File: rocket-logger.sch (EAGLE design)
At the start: 57 parts, among them IC1 CC430F513X, U1 MAX1555, X1 0896BM15A0001, X2 USB-MICROB, X3 SMA-142-0701-801/806

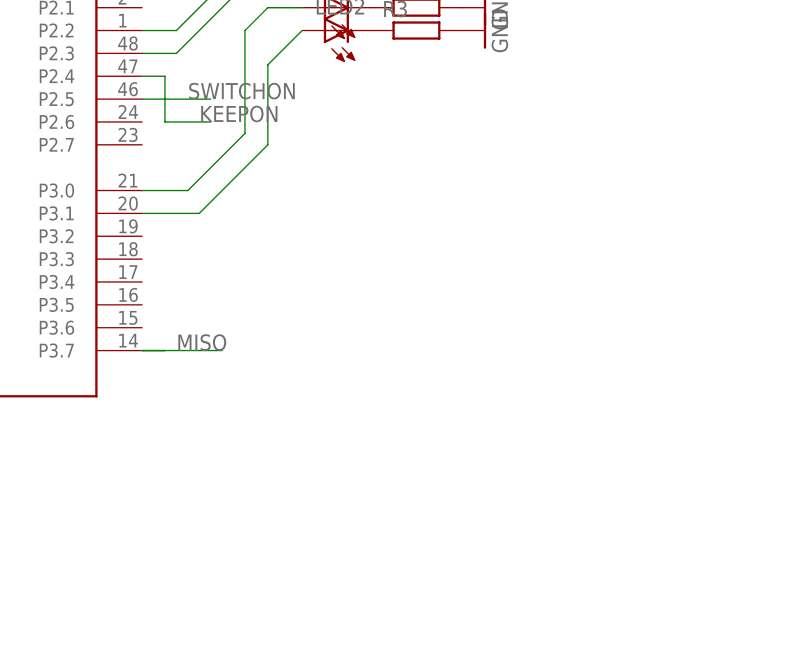
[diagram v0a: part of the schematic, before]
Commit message: now with added flash
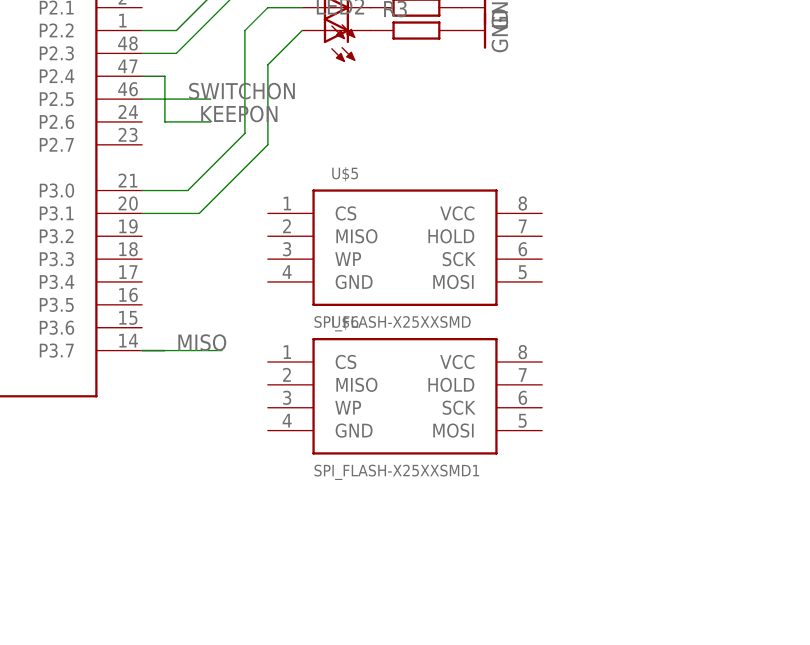
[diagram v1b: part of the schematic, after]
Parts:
- added U$5: SPI_FLASH-X25XXSMD, SparkFun:SPI_FLASH-X25XXSMD
- added U$6: SPI_FLASH-X25XXSMD1, SparkFun:SPI_FLASH-X25XXSMD1
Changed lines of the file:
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@@
 <part name="D4" library="diode" deviceset="DIODE-" device="SOD523"/>
 <part name="R5" library="rcl" deviceset="R-EU_" device="R0402"/>
+<part name="U$5" library="SparkFun" deviceset="SPI_FLASH-X25XX" device="SMD"/>
+<part name="U$6" library="SparkFun" deviceset="SPI_FLASH-X25XX" device="SMD1"/>
 </parts>
 <sheets>
@@
 <instance part="D4" gate="G$1" x="160.02" y="209.55" rot="R180"/>
 <instance part="R5" gate="G$1" x="168.91" y="191.77" rot="R180"/>
+<instance part="U$5" gate="G$1" x="95.25" y="124.46"/>
+<instance part="U$6" gate="G$1" x="95.25" y="107.95"/>
 </instances>
 <busses>

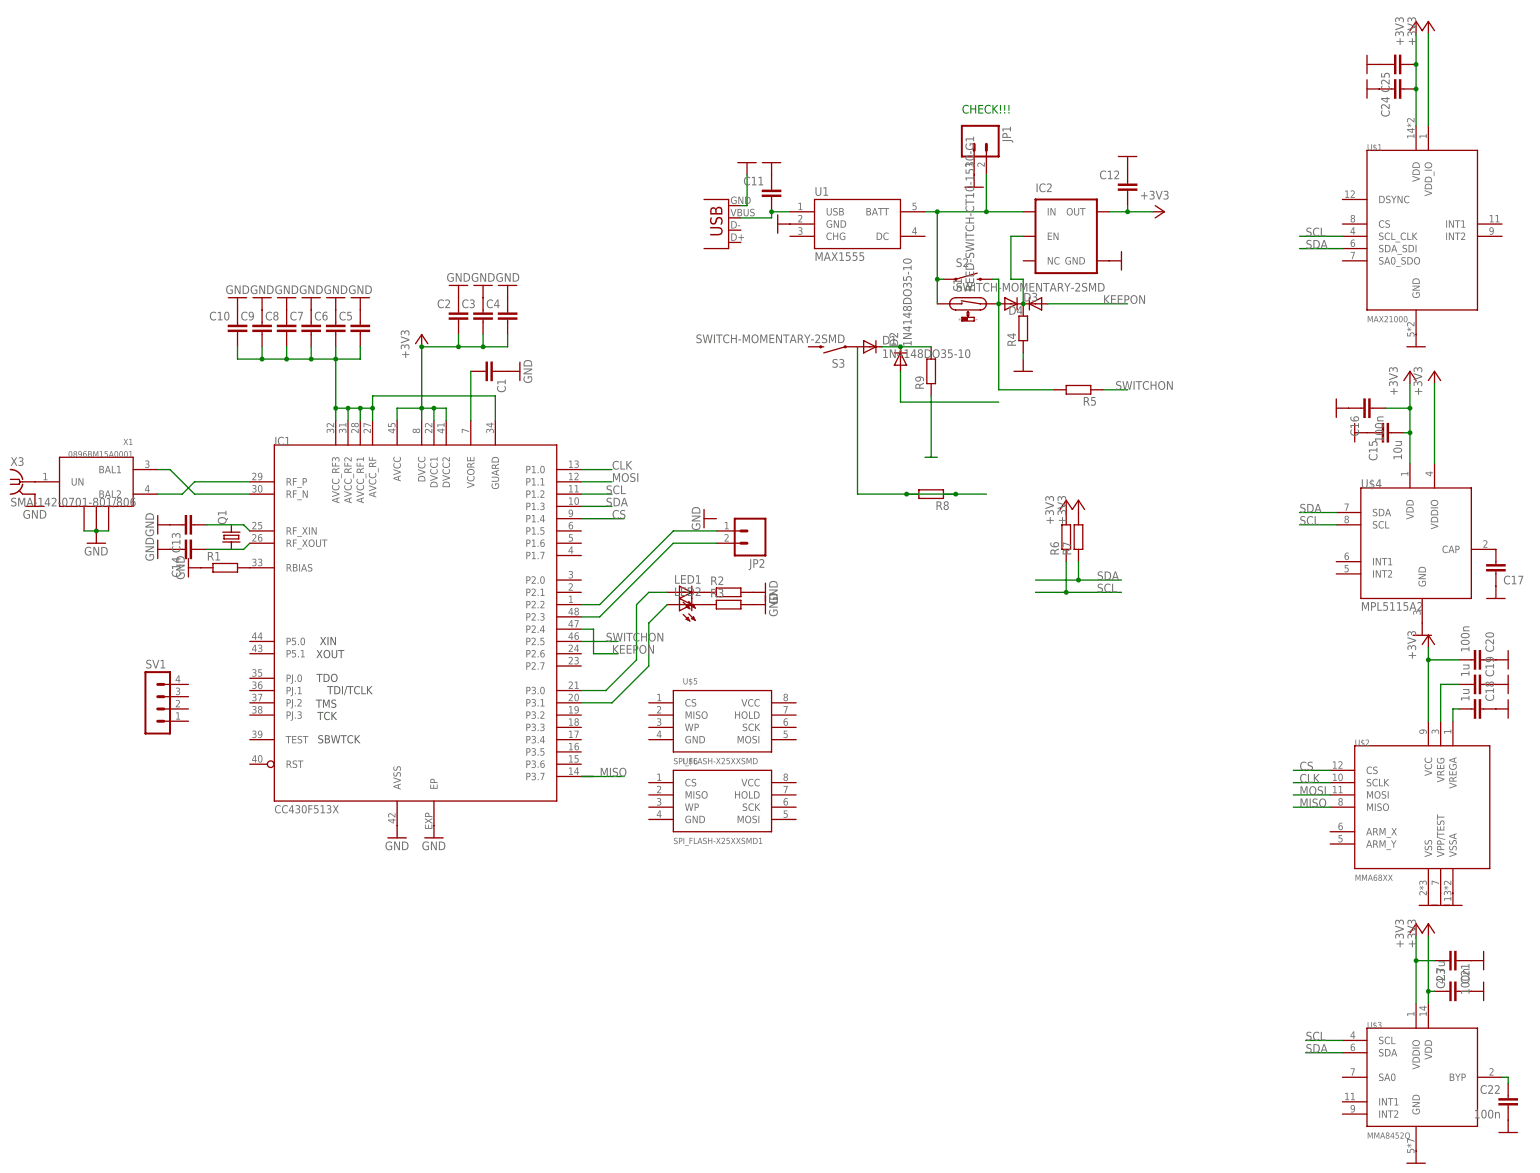
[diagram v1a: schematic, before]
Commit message: added sounder layout
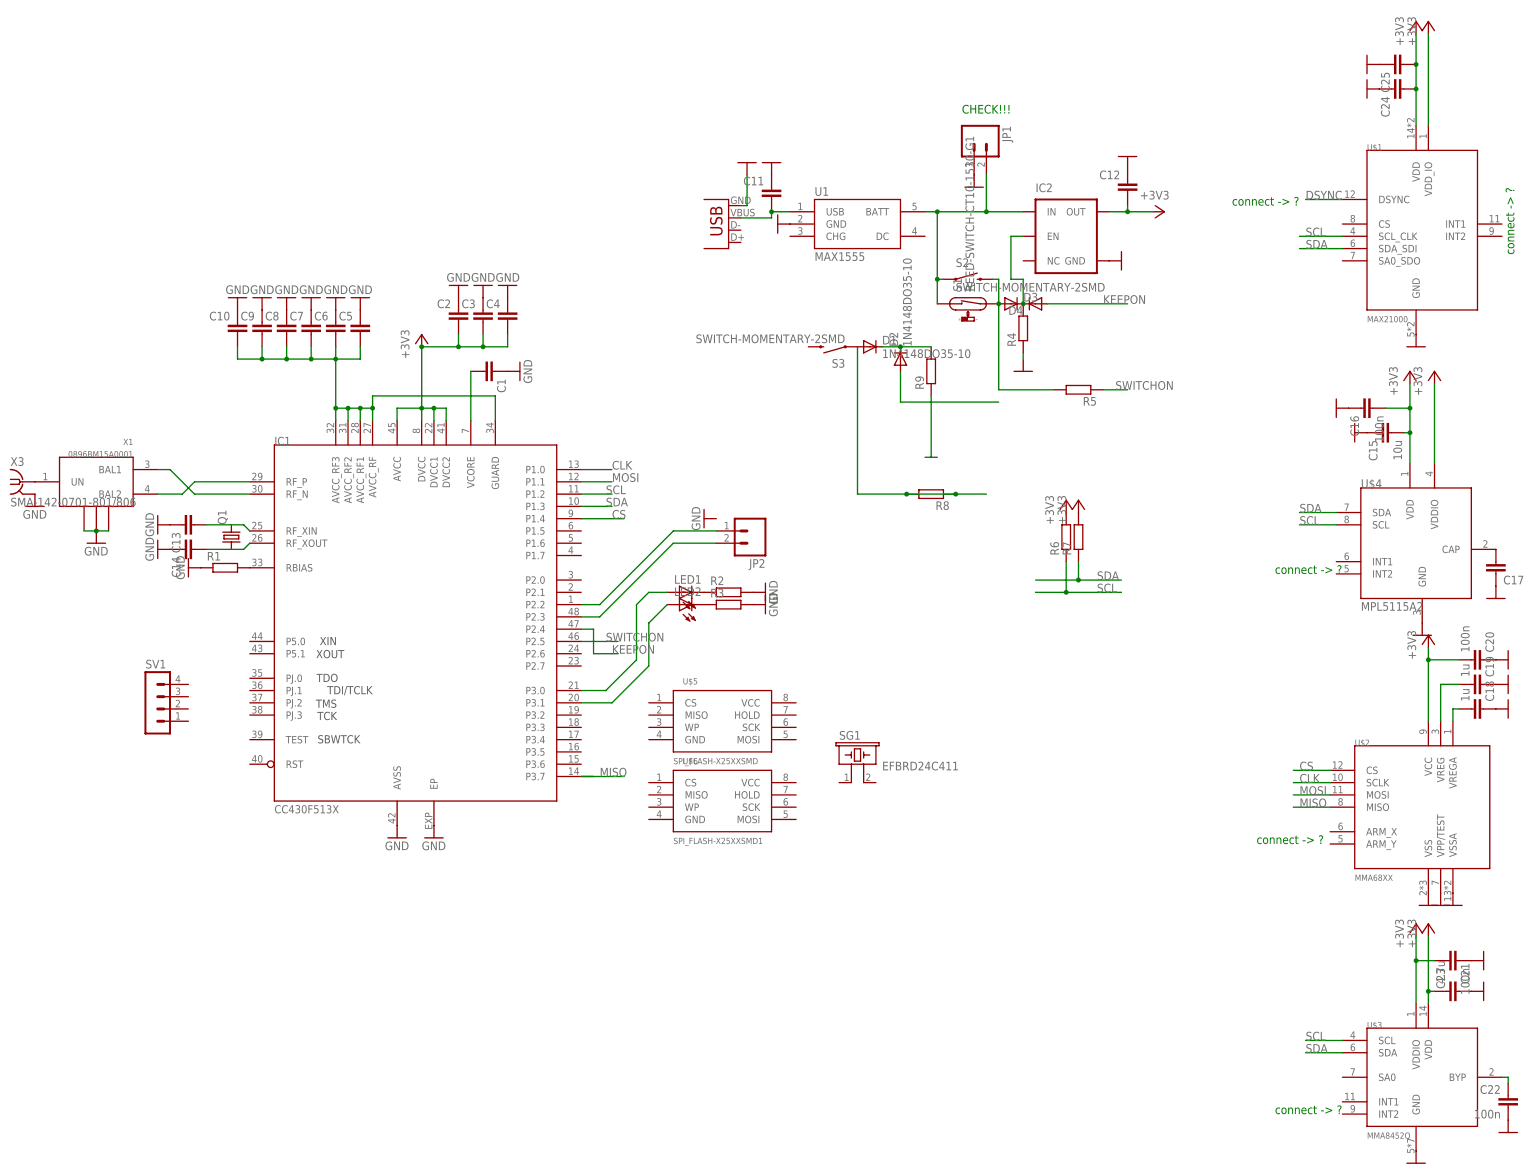
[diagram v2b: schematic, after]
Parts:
- added SG1: EFBRD24C411, buzzer:EFBRD24C411
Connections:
- new net DSYNC: U$1.DSYNC
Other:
- note added: "connect -> ?"
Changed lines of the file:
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@@
 <part name="U$5" library="SparkFun" deviceset="SPI_FLASH-X25XX" device="SMD"/>
 <part name="U$6" library="SparkFun" deviceset="SPI_FLASH-X25XX" device="SMD1"/>
+<part name="SG1" library="buzzer" deviceset="EFB?" device="RD24C411"/>
 </parts>
 <sheets>
@@
 <plain>
 <text x="144.78" y="248.92" size="1.778" layer="91">CHECK!!!</text>
+<text x="200.66" y="229.87" size="1.778" layer="91">connect -&gt; ?</text>
+<text x="209.55" y="153.67" size="1.778" layer="91">connect -&gt; ?</text>
+<text x="205.74" y="97.79" size="1.778" layer="91">connect -&gt; ?</text>
+<text x="209.55" y="41.91" size="1.778" layer="91">connect -&gt; ?</text>
+<text x="259.08" y="219.71" size="1.778" layer="91" rot="R90">connect -&gt; ?</text>
 </plain>
 <instances>
@@
 <instance part="U$5" gate="G$1" x="95.25" y="124.46"/>
 <instance part="U$6" gate="G$1" x="95.25" y="107.95"/>
+<instance part="SG1" gate="G$1" x="121.92" y="113.03"/>
 </instances>
 <busses>
@@
 </segment>
 </net>
+<net name="DSYNC" class="0">
+<segment>
+<pinref part="U$1" gate="G$1" pin="DSYNC"/>
+<wire x1="223.52" y1="231.14" x2="215.9" y2="231.14" width="0.1524" layer="91"/>
+<label x="215.9" y="231.14" size="1.778" layer="95"/>
+</segment>
+</net>

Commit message: moving stuff around a bit
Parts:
- added S4: SWITCH-MOMENTARY-2SMD, SparkFun:SWITCH-MOMENTARY-2SMD
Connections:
- new net CS_F: IC1.P2.0, U$6.CS
- new net HOLD: IC1.P1.7, U$6.HOLD
- new net N$27: U$6.WP
- net +3V3: now also U$6.VCC
- net CLK: now also U$6.SCK
- net GND: now also U$6.GND
- net MISO: now also U$6.MISO
- net MOSI: now also U$6.MOSI
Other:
- moved on the sheet: U$5, U$6
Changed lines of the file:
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@@
 <?xml version="1.0" encoding="utf-8"?>
 <!DOCTYPE eagle SYSTEM "eagle.dtd">
-<eagle version="6.2">
+<eagle version="6.4">
 <drawing>
 <settings>
@@
 <part name="U$6" library="SparkFun" deviceset="SPI_FLASH-X25XX" device="SMD1"/>
 <part name="SG1" library="buzzer" deviceset="EFB?" device="RD24C411"/>
+<part name="S4" library="SparkFun" deviceset="SWITCH-MOMENTARY-2" device="SMD"/>
+<part name="+3V12" library="supply1" deviceset="+3V3" device=""/>
+<part name="GND45" library="SparkFun" deviceset="GND" device=""/>
 </parts>
 <sheets>
@@
 <instance part="D4" gate="G$1" x="160.02" y="209.55" rot="R180"/>
 <instance part="R5" gate="G$1" x="168.91" y="191.77" rot="R180"/>
-<instance part="U$5" gate="G$1" x="95.25" y="124.46"/>
-<instance part="U$6" gate="G$1" x="95.25" y="107.95"/>
+<instance part="U$5" gate="G$1" x="173.99" y="88.9"/>
+<instance part="U$6" gate="G$1" x="176.53" y="128.27"/>
 <instance part="SG1" gate="G$1" x="121.92" y="113.03"/>
+<instance part="S4" gate="G$1" x="87.63" y="189.23"/>
+<instance part="+3V12" gate="G$1" x="194.31" y="130.81" rot="R270"/>
+<instance part="GND45" gate="1" x="158.75" y="123.19" smashed="yes" rot="R270"/>
 </instances>
 <busses>
@@
 <wire x1="157.48" y1="198.12" x2="157.48" y2="199.39" width="0.1524" layer="91"/>
 </segment>
+<segment>
+<pinref part="U$6" gate="G$1" pin="GND"/>
+<pinref part="GND45" gate="1" pin="GND"/>
+</segment>
 </net>
 <net name="N$1" class="0">
@@
 <pinref part="+3V11" gate="G$1" pin="+3V3"/>
 </segment>
+<segment>
+<pinref part="U$6" gate="G$1" pin="VCC"/>
+<pinref part="+3V12" gate="G$1" pin="+3V3"/>
+</segment>
 </net>
 <net name="N$3" class="0">
@@
 <label x="214.63" y="105.41" size="1.778" layer="95"/>
 </segment>
+<segment>
+<pinref part="U$6" gate="G$1" pin="MISO"/>
+<wire x1="161.29" y1="128.27" x2="149.86" y2="128.27" width="0.1524" layer="91"/>
+<label x="149.86" y="128.27" size="1.778" layer="95"/>
+</segment>
 </net>
 <net name="MOSI" class="0">
@@
 <label x="214.63" y="107.95" size="1.778" layer="95"/>
 </segment>
+<segment>
+<pinref part="U$6" gate="G$1" pin="MOSI"/>
+<wire x1="191.77" y1="123.19" x2="201.93" y2="123.19" width="0.1524" layer="91"/>
+<label x="196.85" y="123.19" size="1.778" layer="95"/>
+</segment>
 </net>
 <net name="CLK" class="0">
@@
 <wire x1="220.98" y1="110.49" x2="213.36" y2="110.49" width="0.1524" layer="91"/>
 <label x="214.63" y="110.49" size="1.778" layer="95"/>
+</segment>
+<segment>
+<pinref part="U$6" gate="G$1" pin="SCK"/>
+<wire x1="191.77" y1="125.73" x2="201.93" y2="125.73" width="0.1524" layer="91"/>
+<label x="196.85" y="125.73" size="1.778" layer="95"/>
 </segment>
 </net>
@@
 </segment>
 </net>
+<net name="CS_F" class="0">
+<segment>
+<pinref part="U$6" gate="G$1" pin="CS"/>
+<wire x1="161.29" y1="130.81" x2="149.86" y2="130.81" width="0.1524" layer="91"/>
+<label x="149.86" y="130.81" size="1.778" layer="95"/>
+</segment>
+<segment>
+<pinref part="IC1" gate="G$1" pin="P2.0"/>
+<wire x1="66.04" y1="152.4" x2="71.12" y2="152.4" width="0.1524" layer="91"/>
+<label x="71.12" y="152.4" size="1.778" layer="95"/>
+</segment>
+</net>
+<net name="N$27" class="0">
+<segment>
+<pinref part="U$6" gate="G$1" pin="WP"/>
+<wire x1="161.29" y1="125.73" x2="149.86" y2="125.73" width="0.1524" layer="91"/>
+<label x="149.86" y="125.73" size="1.778" layer="95"/>
+</segment>
+</net>
+<net name="HOLD" class="0">
+<segment>
+<pinref part="U$6" gate="G$1" pin="HOLD"/>
+<wire x1="191.77" y1="128.27" x2="201.93" y2="128.27" width="0.1524" layer="91"/>
+<label x="196.85" y="128.27" size="1.778" layer="95"/>
+</segment>
+<segment>
+<pinref part="IC1" gate="G$1" pin="P1.7"/>
+<wire x1="66.04" y1="157.48" x2="72.39" y2="157.48" width="0.1524" layer="91"/>
+<label x="71.12" y="157.48" size="1.778" layer="95"/>
+</segment>
+</net>
